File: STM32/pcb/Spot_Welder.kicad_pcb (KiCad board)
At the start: 2 copper layers, 100 x 90 mm, 89 parts, among them J1 SSD1306, J2 Debug, J5 Battery, J6 Foot_Switch, SW1 RE, U1 HY4903B6, U10 HY4903B6, U11 HY4903B6, U12 24LC64, U2 STM32F030F4Px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

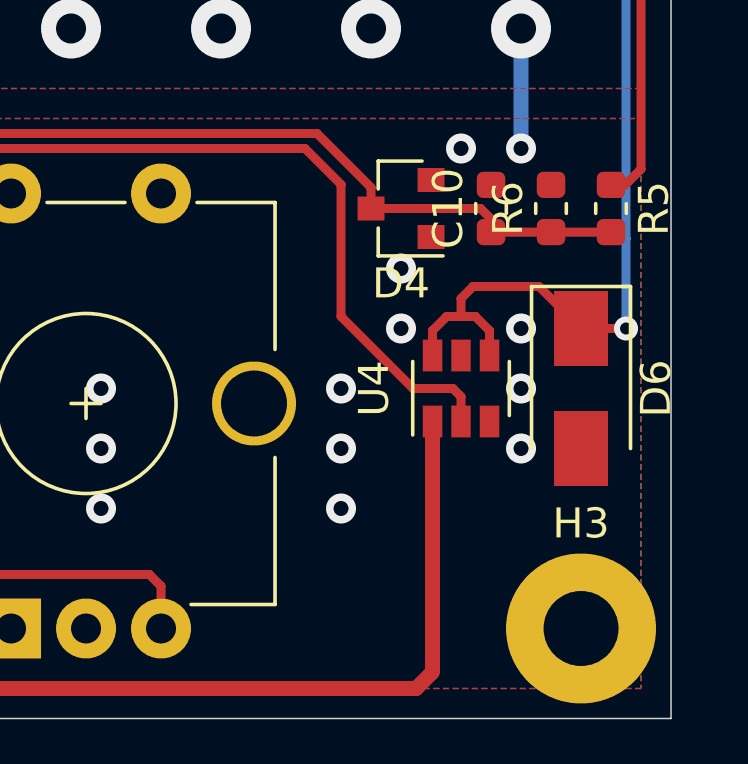
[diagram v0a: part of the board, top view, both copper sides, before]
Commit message: gate driver changed to mcp1416
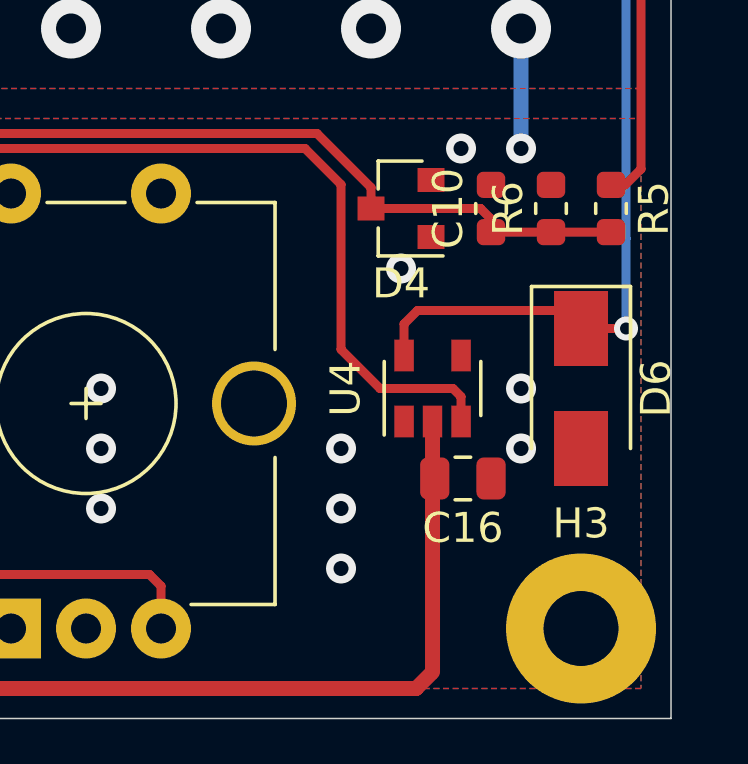
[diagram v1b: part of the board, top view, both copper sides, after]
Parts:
- added C16: 10u, Capacitor_SMD:C_0805_2012Metric, F.Cu at (173.1, 172.0)
- R13, R14, R15, R16, R17, R18, R19, R20: value 22 -> 100
- U4: value ZXGD3009E6 -> MCP1416; footprint Package_TO_SOT_SMD:SOT-23-6 -> Package_TO_SOT_SMD:SOT-23-5
- moved U4 0.95 mm to (172.1, 169.0)
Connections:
- U4 pad 1: 12V_VCC -> Net-(U4-Pad1)
- U4 pad 2: MCU_Gate -> 12V_VCC
- U4 pad 3: GND -> MCU_Gate
- U4 pad 4: Gate_Drive -> GND
- U4 pad 5: Net-(U4-Pad5) -> Gate_Drive
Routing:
- net Gate_Drive: track 157.5 -> 155.5 mm
- net MCU_Gate: track 61.1 -> 61.7 mm
- net GND: vias 133 -> 131
